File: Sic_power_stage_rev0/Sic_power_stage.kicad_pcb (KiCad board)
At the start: 4 copper layers, 242.5 x 94.5 mm, 153 parts, among them J1 20021321-00006C4LF, J2 20021321-00006C4LF, J3 20021321-00006C4LF, J4 20021321-00006C4LF, J5 20021321-00006C4LF, J6 20021321-00006C4LF, J7 20021321-00006C4LF, J8 20021321-00006C4LF, Q1 NTBG014N120M3P, Q10 NTBG014N120M3P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

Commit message: Sic: Add more vias on Leg A
Signed-off-by: Ayarde Christian <cayarde@paltatech.com>
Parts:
- R48: footprint IPC7351-Nominal:RESC3216X60 -> Resistor_SMD:R_0603_1608Metric
- moved U1 210.5 mm to (-115.6, 30.2)
- moved R48 186.7 mm to (-116.2, 27.5), turned to 180 degrees
- moved C5 0.25 mm to (-70.5, -19.2)
- moved C6 0.25 mm to (-70.5, -13.2)
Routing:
- net /Half Bridge A/NTC_BOT: track 51.5 -> 56.0 mm
- net VBUS: vias 1849 -> 2337
- net /Half Bridge A/node_a: vias 331 -> 1037

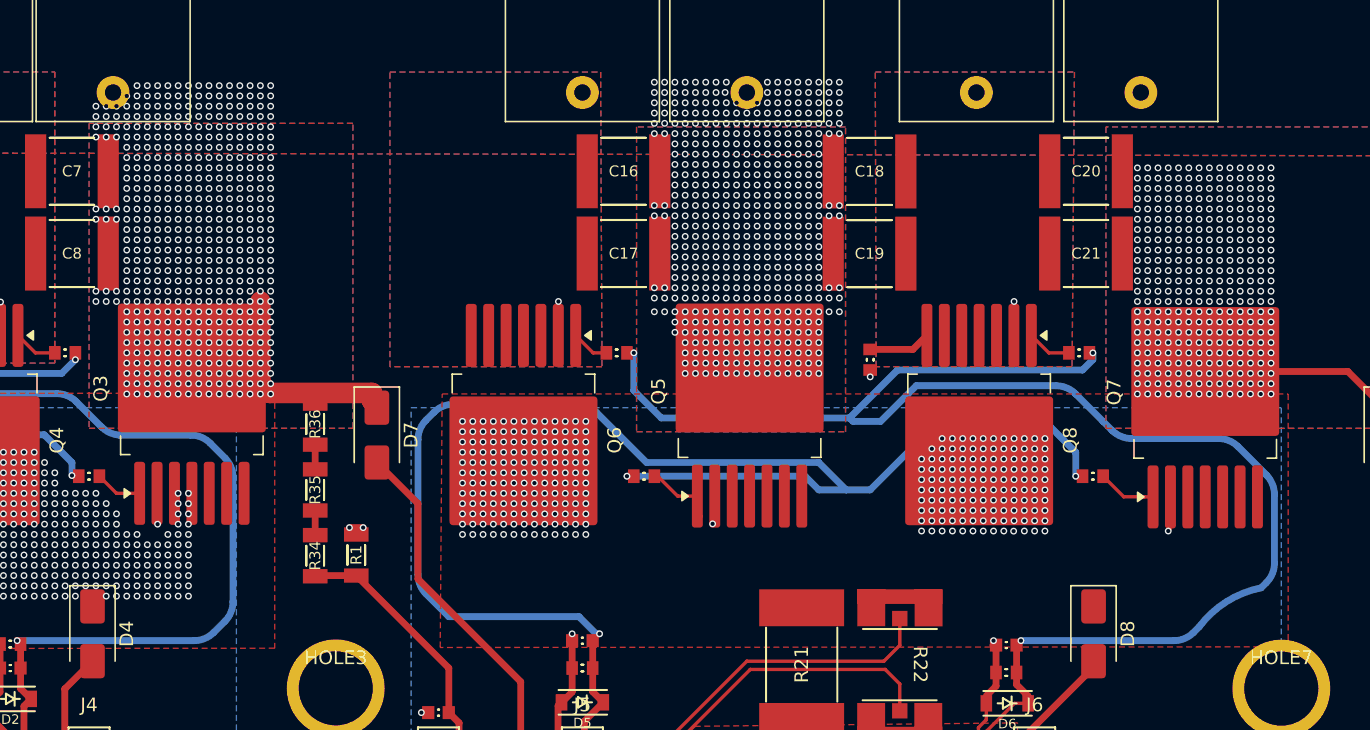
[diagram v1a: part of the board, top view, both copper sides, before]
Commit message: Sic: Add vias on leg B
Signed-off-by: Ayarde Christian <cayarde@paltatech.com>
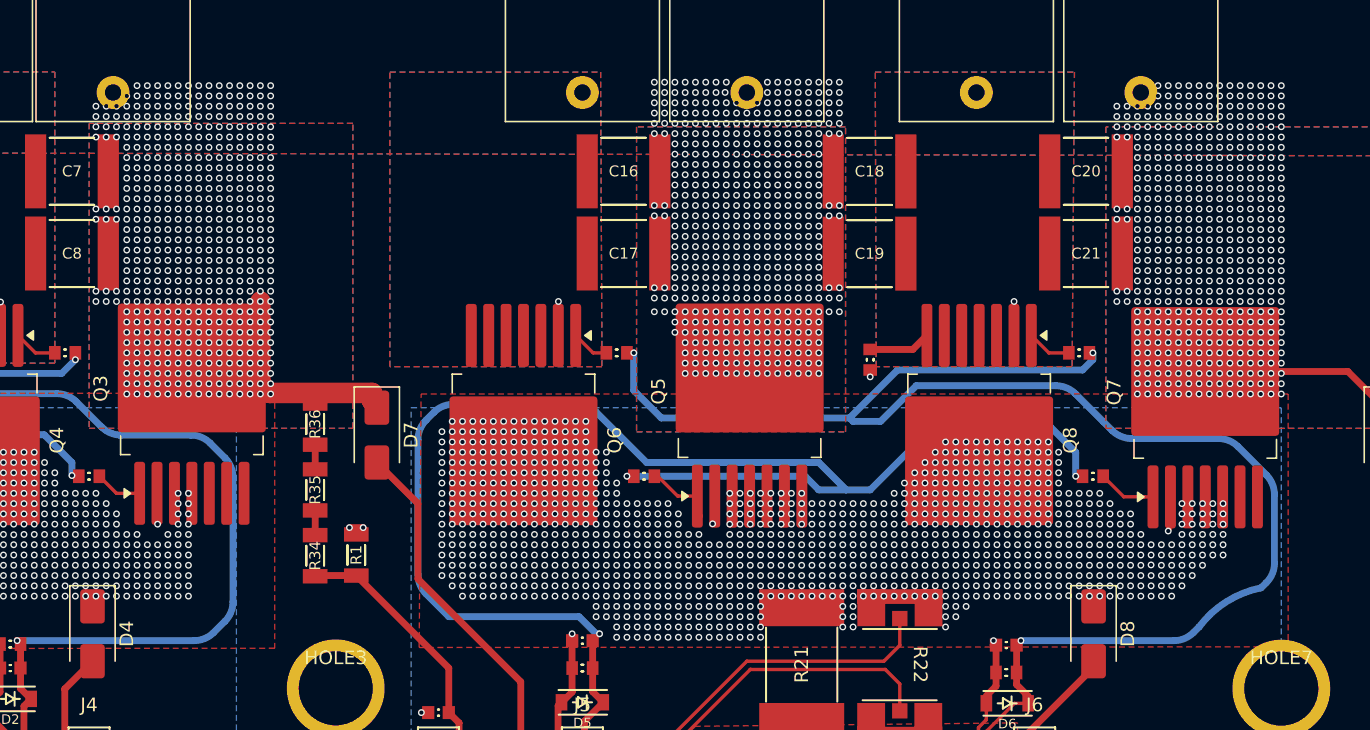
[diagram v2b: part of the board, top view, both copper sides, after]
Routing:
- net /Half Bridge A/NTC_BOT: track 56.0 -> 57.6 mm
- net VBUS: vias 2337 -> 2492
- net /Half Bridge B/node_a: vias 283 -> 1026
- net /Half Bridge A/node_a: vias 1037 -> 1039

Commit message: Sic: Add vias on leg C
Signed-off-by: Ayarde Christian <cayarde@paltatech.com>
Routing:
- net /Half Bridge C/NTC_BOT: track 44.2 -> 55.2 mm
- net /Half Bridge A/S_BOT: track 136.5 -> 138.5 mm
- net /Half Bridge A/G_BOT: track 111.5 -> 113.3 mm
- net /Half Bridge A/NTC_BOT: track 57.6 -> 58.7 mm
- net /Half Bridge C/node_a: vias 247 -> 982
- net /Half Bridge C/S_TOP: vias 2 -> 3
- net /Half Bridge B/node_a: vias 1026 -> 1023
- net /Half Bridge A/node_a: vias 1039 -> 1058

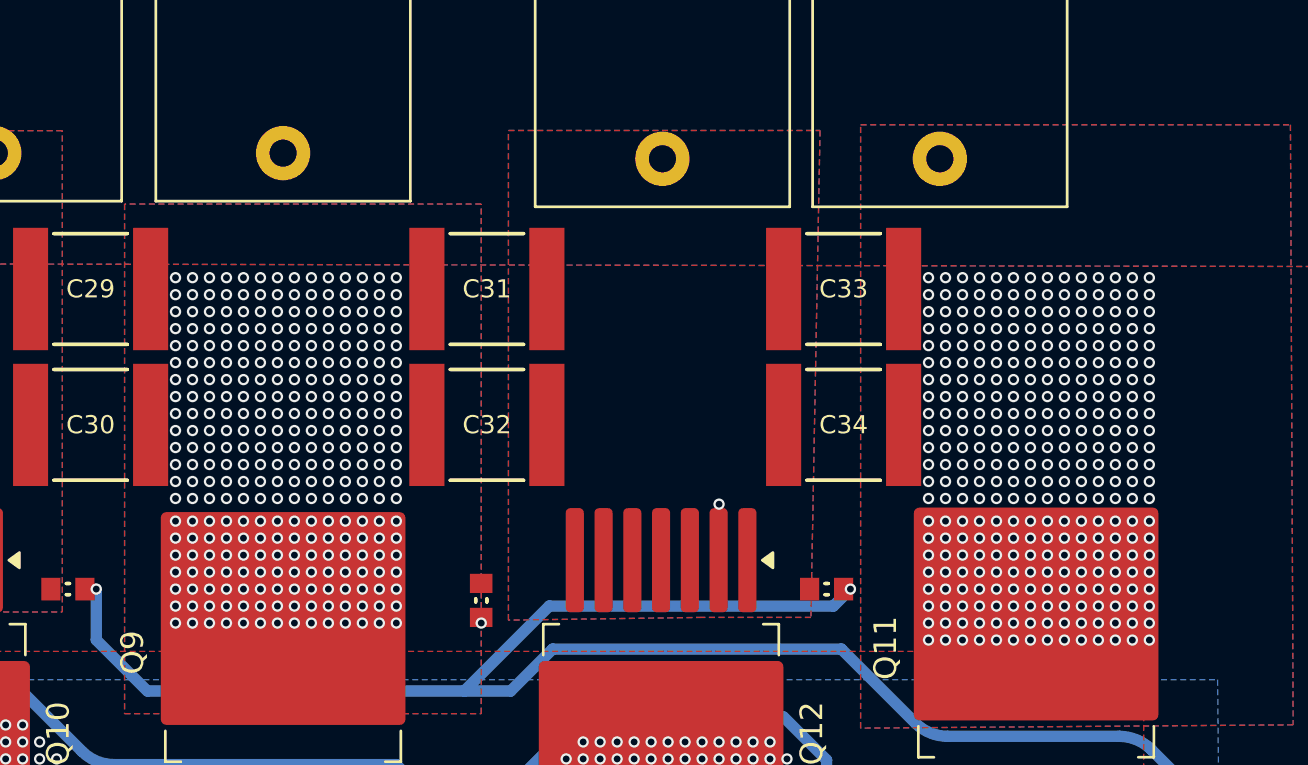
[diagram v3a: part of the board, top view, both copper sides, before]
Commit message: Sic: Vias on Led C - Vbus
Signed-off-by: Ayarde Christian <cayarde@paltatech.com>
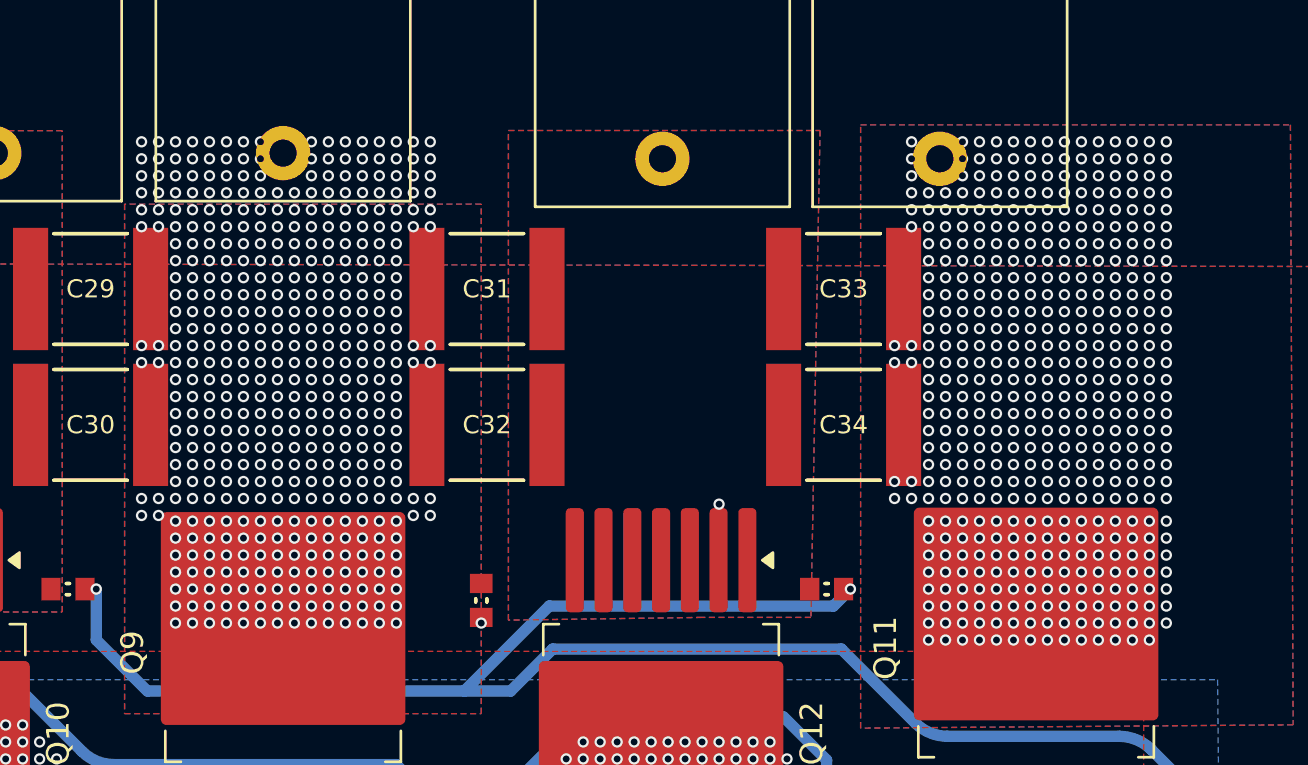
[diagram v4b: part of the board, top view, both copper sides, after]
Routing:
- net VBUS: vias 2492 -> 2787

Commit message: Sic: define resistors value for discharge circuit
Signed-off-by: Ayarde Christian <cayarde@paltatech.com>
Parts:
- moved R3 494.5 mm to (116.5, -3.50), turned to 90 degrees
- moved D13 454.2 mm to (129.8, 22.2)
- moved R40 454.1 mm to (119.0, 1.50), turned to 90 degrees
- moved R42 451.6 mm to (116.5, 6.50), turned to 90 degrees
- moved R45 450.2 mm to (120.0, 19.0), turned to 180 degrees
- moved R41 449.8 mm to (114.0, 6.50)
- moved R43 448.8 mm to (119.0, 6.50), turned to 90 degrees
- moved R2 448.4 mm to (119.0, -3.50), turned to 90 degrees
- moved R39 446.2 mm to (116.5, 1.50), turned to 90 degrees
- moved DS1 445.8 mm to (119.8, 24.5), turned to 90 degrees
- moved R44 445.7 mm to (115.2, 19.0)
- moved R38 443.9 mm to (114.0, 1.50), turned to 90 degrees
- moved R37 443.8 mm to (114.0, -3.50), turned to 90 degrees
- moved Q13 440.1 mm to (117.5, 31.5)
- moved C41 432.9 mm to (110.5, 29.2)
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
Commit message: Sic: Define custom rules for Vbus sense
Signed-off-by: Ayarde Christian <cayarde@paltatech.com>
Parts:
- removed C13, C26, C39: 5uF, Capacitor_THT:C_Rect_L18.0mm_W9.0mm_P15.00mm_FKS3_FKP3
- added J9: Conn_01x01_Pin, Connector_PinHeader_1.00mm:PinHeader_1x01_P1.00mm_Vertical, F.Cu at (105.8, 35.8)
- added R49: 17.6K, IPC7351-Nominal:RESC3216X60, F.Cu at (114.5, -1.51)
- added R50: 17.6K, IPC7351-Nominal:RESC3216X60, F.Cu at (117.8, -1.51)
- added R51: 17.6K, IPC7351-Nominal:RESC3216X60, F.Cu at (121.2, -1.50)
- added R52: 17.6K, IPC7351-Nominal:RESC3216X60, F.Cu at (114.5, 4.00)
- added R53: 17.6K, IPC7351-Nominal:RESC3216X60, F.Cu at (117.8, 4.00)
- added R54: 17.6K, IPC7351-Nominal:RESC3216X60, F.Cu at (121.2, 4.00)
- added R55: 17.6K, IPC7351-Nominal:RESC3216X60, F.Cu at (114.4, 10.0)
- added R56: 17.6K, IPC7351-Nominal:RESC3216X60, F.Cu at (117.8, 10.0)
- added R57: 17.6K, IPC7351-Nominal:RESC3216X60, F.Cu at (121.1, 10.0)
- C41: value C-0603 -> 100n
- R1: value R-1206 -> 5K; footprint IPC7351-Nominal:RESC3216X60 -> Resistor_SMD:R_0603_1608Metric
- R2, R3, R37, R38, R39, R40, R41, R42, R43: value R-1206 -> 17.6K
- R34, R35, R36: value R-1206 -> 220K
- R44, R45, R46: value R-1206 -> 365K
- R47: value R-1206 -> 10R; footprint IPC7351-Nominal:RESC3216X60 -> Resistor_SMD:R_0805_2012Metric
- U1: value TLP785 -> RV1S2281A; footprint Package_DIP:DIP-4_W7.62mm -> Package_SO:SSOP-4_4.4x2.6mm_P1.27mm
- moved R2 15.2 mm to (121.2, -18.5)
- moved R3 15.0 mm to (117.2, -18.5)
- moved R37 15.0 mm to (113.2, -18.5)
- moved R40 14.4 mm to (121.2, -12.8)
- moved R39 14.3 mm to (117.8, -12.8)
- moved R38 14.3 mm to (114.5, -12.8)
- moved R43 13.9 mm to (121.2, -7.25)
- moved R42 13.8 mm to (117.8, -7.25)
- moved R41 13.8 mm to (114.5, -7.25)
- moved R44 3.12 mm to (114.4, 16.0), turned to -90 degrees
- moved R48 2.69 mm to (90.8, 32.0)
- moved R1 0.50 mm to (-33.0, 9.25)
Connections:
- net Net-(R34-Pad2) renamed /Discharge_circuit and Vbus resistor/PHASE_HV_A_2
- net Net-(R35-Pad2) renamed /Discharge_circuit and Vbus resistor/PHASE_HV_A_1
- R41 pad 1: Net-(DS1-A) -> Net-(R41-Pad1)
- R42 pad 1: Net-(DS1-A) -> Net-(R41-Pad1)
- R43 pad 1: Net-(DS1-A) -> Net-(R41-Pad1)
- U1 pad 2: /Discharge_circuit and Vbus resistor/GND -> PWRGND
